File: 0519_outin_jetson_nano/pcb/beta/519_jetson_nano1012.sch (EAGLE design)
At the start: 94 parts, among them P1 MF-NSML600-2, U2 TXB0108, U7 LP2985-50

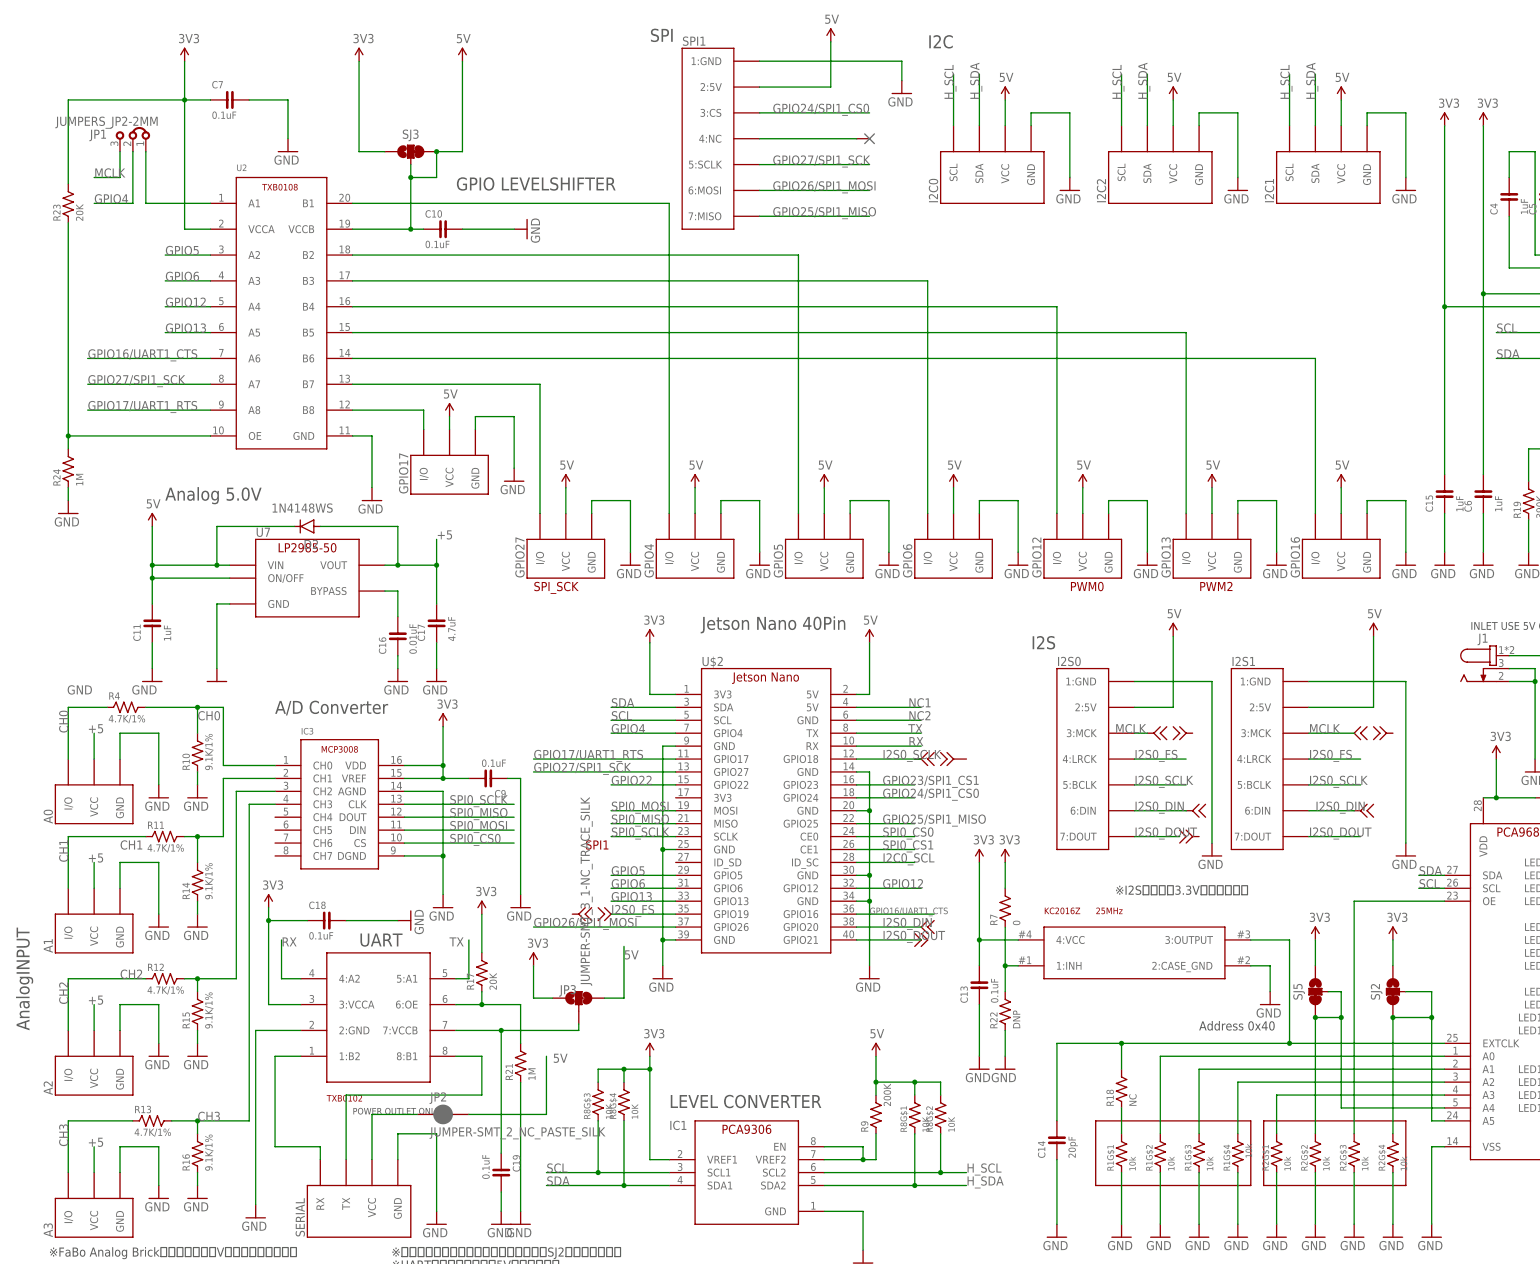
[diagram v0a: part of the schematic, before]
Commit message: #519 Jetson OUTIN DCプラグ変更、GPIO27信号切り替え追加、アナログADC電源を3.3Vに変更。
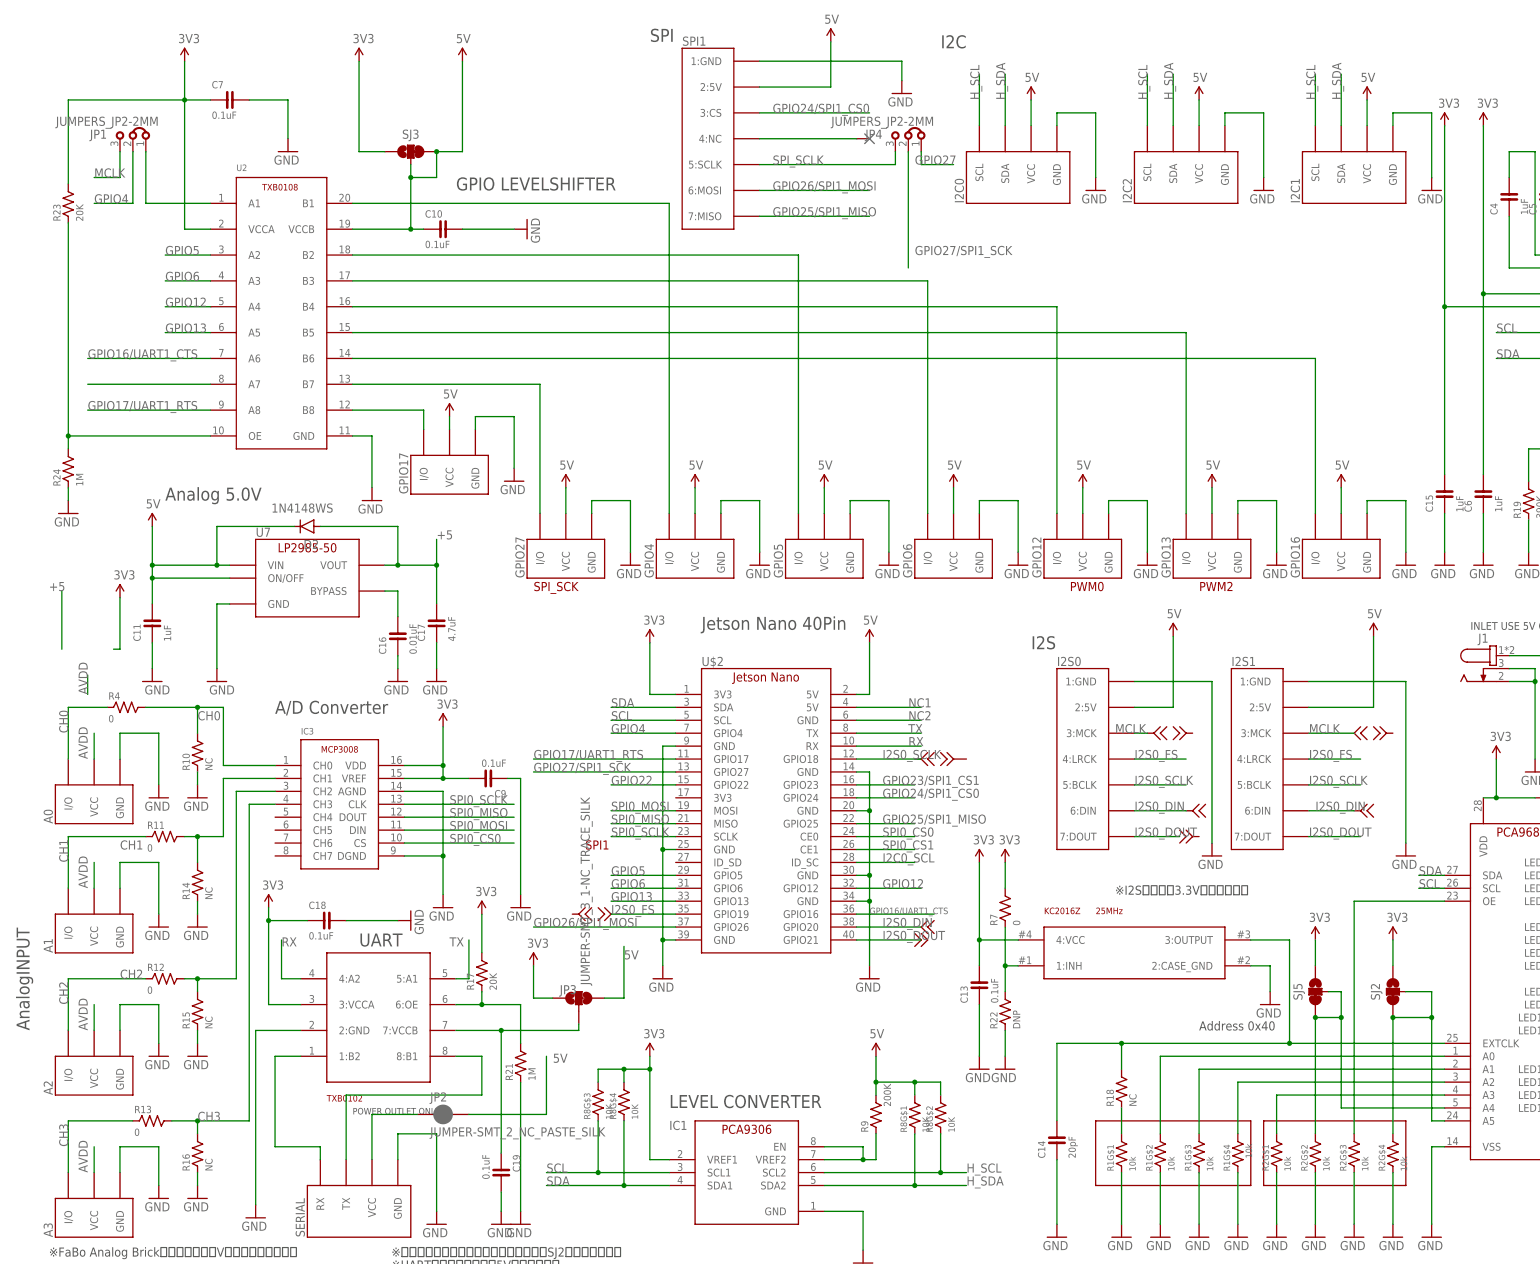
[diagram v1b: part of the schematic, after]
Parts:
- added JP4: JUMPERS_JP2-2MM, 52101-101-REV-A_v16:JUMPERS_JP2-2MM
- R10, R14, R15, R16: value 9.1K/1% -> NC
- R11, R12, R13, R4: value 4.7K/1% -> 0
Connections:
- new net AVDD: A0.VCC, A1.VCC, A2.VCC, A3.VCC
- new net GPIO27: JP4G$1.1, U2.A7
- new net SPI_SCLK: JP4G$1.3, SPI1.5:SCLK
- net +5: no longer A0.VCC, A1.VCC, A2.VCC, A3.VCC
- net GPIO27/SPI1_SCK: now also JP4G$1.2; no longer SPI1.5:SCLK, U2.A7
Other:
- moved on the sheet: I2C0, I2C1, I2C2
